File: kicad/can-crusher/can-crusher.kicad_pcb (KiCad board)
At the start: 2 copper layers, 100 x 100 mm, 21 parts, among them J1 Stepper Right, J2 Control UART, J3 Ext power, J4 Stepper Left, J5 Barrel_Jack, J6 Expansion Port, Q1 IRF9540N, Q2 BS170, SW1 Reboot, SW2 User Interaction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

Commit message: Add pull down to power circuitry
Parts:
- added R8: 57.6k, Resistor_THT:R_Axial_DIN0207_L6.3mm_D2.5mm_P10.16mm_Horizontal, F.Cu at (175.3, 105.4)
- R6: value 50k -> 57.6k
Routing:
- net Net-(Q2-Pad2): track 129.9 -> 140.6 mm
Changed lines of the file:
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@@
       (effects (font (size 1 1) (thickness 0.15)))
     )
-    (fp_text value "50k" (at 7.62 -2.54) (layer "F.Fab")
+    (fp_text value "57.6k" (at 7.62 -2.54) (layer "F.Fab")
       (effects (font (size 1 1) (thickness 0.15)))
     )
@@
       (net 1 "GND") (pinfunction "Pin_2") (pintype "passive"))
     (model "${KICAD6_3DMODEL_DIR}/Connector_PinHeader_2.54mm.3dshapes/PinHeader_1x02_P2.54mm_Vertical.wrl"
+      (offset (xyz 0 0 0))
+      (scale (xyz 1 1 1))
+      (rotate (xyz 0 0 0))
+    )
+  )
+  (footprint "Resistor_THT:R_Axial_DIN0207_L6.3mm_D2.5mm_P10.16mm_Horizontal" (layer "F.Cu")
+    (at 175.26 105.41)
+    (descr "Resistor, Axial_DIN0207 series, Axial, Horizontal, pin pitch=10.16mm, 0.25W = 1/4W, length*diameter=6.3*2.5mm^2, http://cdn-reichelt.de/documents/datenblatt/B400/1_4W%23YAG.pdf")
+    (tags "Resistor Axial_DIN0207 series Axial Horizontal pin pitch 10.16mm 0.25W = 1/4W length 6.3mm diameter 2.5mm")
+    (property "Sheetfile" "File: can-crusher.kicad_sch")
+    (property "Sheetname" "")
+    (attr through_hole)
+    (fp_text reference "R8" (at 5.08 -2.37) (layer "F.SilkS")
+      (effects (font (size 1 1) (thickness 0.15)))
+    )
+    (fp_text value "57.6k" (at 5.08 2.37) (layer "F.Fab")
+      (effects (font (size 1 1) (thickness 0.15)))
+    )
+    (fp_text user "${REFERENCE}" (at 5.08 0) (layer "F.Fab")
+      (effects (font (size 1 1) (thickness 0.15)))
+    )
+    (fp_line (start 9.12 0) (end 8.35 0) (layer "F.SilkS") (width 0.12))
+    (fp_line (start 8.35 -1.37) (end 1.81 -1.37) (layer "F.SilkS") (width 0.12))
+    (fp_line (start 1.81 -1.37) (end 1.81 1.37) (layer "F.SilkS") (width 0.12))
+    (fp_line (start 1.04 0) (end 1.81 0) (layer "F.SilkS") (width 0.12))
+    (fp_line (start 1.81 1.37) (end 8.35 1.37) (layer "F.SilkS") (width 0.12))
+    (fp_line (start 8.35 1.37) (end 8.35 -1.37) (layer "F.SilkS") (width 0.12))
+    (fp_line (start 11.21 -1.5) (end -1.05 -1.5) (layer "F.CrtYd") (width 0.05))
+    (fp_line (start 11.21 1.5) (end 11.21 -1.5) (layer "F.CrtYd") (width 0.05))
+    (fp_line (start -1.05 -1.5) (end -1.05 1.5) (layer "F.CrtYd") (width 0.05))
+    (fp_line (start -1.05 1.5) (end 11.21 1.5) (layer "F.CrtYd") (width 0.05))
+    (fp_line (start 8.23 1.25) (end 8.23 -1.25) (layer "F.Fab") (width 0.1))
+    (fp_line (start 10.16 0) (end 8.23 0) (layer "F.Fab") (width 0.1))
+    (fp_line (start 1.93 -1.25) (end 1.93 1.25) (layer "F.Fab") (width 0.1))
+    (fp_line (start 0 0) (end 1.93 0) (layer "F.Fab") (width 0.1))
+    (fp_line (start 1.93 1.25) (end 8.23 1.25) (layer "F.Fab") (width 0.1))
+    (fp_line (start 8.23 -1.25) (end 1.93 -1.25) (layer "F.Fab") (width 0.1))
+    (pad "1" thru_hole circle (at 0 0) (size 1.6 1.6) (drill 0.8) (layers *.Cu *.Mask)
+      (net 27 "Net-(Q2-Pad2)") (pintype "passive"))
+    (pad "2" thru_hole oval (at 10.16 0) (size 1.6 1.6) (drill 0.8) (layers *.Cu *.Mask)
+      (net 1 "GND") (pintype "passive"))
+    (model "${KICAD6_3DMODEL_DIR}/Resistor_THT.3dshapes/R_Axial_DIN0207_L6.3mm_D2.5mm_P10.16mm_Horizontal.wrl"
       (offset (xyz 0 0 0))
       (scale (xyz 1 1 1))
@@
   (segment (start 183.92 97.16) (end 189 92.08) (width 0.25) (layer "F.Cu") (net 26))
   (segment (start 184.78 92.08) (end 189 92.08) (width 0.25) (layer "F.Cu") (net 26))
+  (segment (start 176.53 95.25) (end 176.53 104.14) (width 0.25) (layer "F.Cu") (net 27))
   (segment (start 175.26 80.01) (end 175.26 88.9) (width 0.25) (layer "F.Cu") (net 27))
   (segment (start 133.35 120.65) (end 130.81 118.11) (width 0.25) (layer "F.Cu") (net 27))
@@
   (segment (start 176.53 90.17) (end 176.53 95.25) (width 0.25) (layer "F.Cu") (net 27))
   (segment (start 138.43 120.65) (end 133.35 120.65) (width 0.25) (layer "F.Cu") (net 27))
+  (segment (start 176.53 104.14) (end 175.26 105.41) (width 0.25) (layer "F.Cu") (net 27))
   (segment (start 130.81 115.57) (end 116.84 101.6) (width 0.25) (layer "F.Cu") (net 27))
   (segment (start 116.84 80.01) (end 120.65 76.2) (width 0.25) (layer "F.Cu") (net 27))
@@
     (connect_pads (clearance 0.508))
     (min_thickness 0.254) (filled_areas_thickness no)
-    (fill (thermal_gap 0.508) (thermal_bridge_width 0.508))
+    (fill yes (thermal_gap 0.508) (thermal_bridge_width 0.508))
     (polygon
       (pts

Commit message: Add mounting holes
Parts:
- added REF1: MountingHole_3mm_Pad, MountingHole:MountingHole_3mm_Pad, F.Cu at (101.6, 57.1)
- added REF2: MountingHole_3mm_Pad, MountingHole:MountingHole_3mm_Pad, F.Cu at (177.8, 57.1)
- added REF3: MountingHole_3mm_Pad, MountingHole:MountingHole_3mm_Pad, F.Cu at (191.8, 135.9)
- added REF4: MountingHole_3mm_Pad, MountingHole:MountingHole_3mm_Pad, F.Cu at (101.6, 146.1)
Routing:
- net +3.3V: track 179.5 -> 177.7 mm
- net GND: vias 22 -> 16
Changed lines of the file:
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@@
   (net 55 "Net-(D1-Pad2)")
   (net 56 "Net-(D1-Pad4)")
+  (footprint "MountingHole:MountingHole_3mm_Pad" (layer "F.Cu")
+    (at 191.77 135.89)
+    (descr "Mounting Hole 3mm")
+    (tags "mounting hole 3mm")
+    (attr exclude_from_pos_files exclude_from_bom)
+    (fp_text reference "REF3" (at 0 -4) (layer "Cmts.User")
+      (effects (font (size 1 1) (thickness 0.15)))
+    )
+    (fp_text value "MountingHole_3mm_Pad" (at 0 4) (layer "F.Fab")
+      (effects (font (size 1 1) (thickness 0.15)))
+    )
+    (fp_text user "${REFERENCE}" (at 0 0) (layer "F.Fab")
+      (effects (font (size 1 1) (thickness 0.15)))
+    )
+    (fp_circle (center 0 0) (end 3 0) (layer "Cmts.User") (width 0.15) (fill none))
+    (fp_circle (center 0 0) (end 3.25 0) (layer "F.CrtYd") (width 0.05) (fill none))
+    (pad "1" thru_hole circle (at 0 0) (size 6 6) (drill 3) (layers *.Cu *.Mask))
+  )
+  (footprint "MountingHole:MountingHole_3mm_Pad" (layer "F.Cu")
+    (at 177.8 57.15)
+    (descr "Mounting Hole 3mm")
+    (tags "mounting hole 3mm")
+    (attr exclude_from_pos_files exclude_from_bom)
+    (fp_text reference "REF2" (at 0 -4) (layer "Cmts.User")
+      (effects (font (size 1 1) (thickness 0.15)))
+    )
+    (fp_text value "MountingHole_3mm_Pad" (at 0 4) (layer "F.Fab")
+      (effects (font (size 1 1) (thickness 0.15)))
+    )
+    (fp_text user "${REFERENCE}" (at 0 0) (layer "F.Fab")
+      (effects (font (size 1 1) (thickness 0.15)))
+    )
+    (fp_circle (center 0 0) (end 3 0) (layer "Cmts.User") (width 0.15) (fill none))
+    (fp_circle (center 0 0) (end 3.25 0) (layer "F.CrtYd") (width 0.05) (fill none))
+    (pad "1" thru_hole circle (at 0 0) (size 6 6) (drill 3) (layers *.Cu *.Mask))
+  )
   (footprint "Package_TO_SOT_THT:TO-220-3_Vertical" (layer "F.Cu")
     (at 189 92.08 90)
@@
       (rotate (xyz 0 0 0))
     )
+  )
+  (footprint "MountingHole:MountingHole_3mm_Pad" (layer "F.Cu")
+    (at 101.6 146.05)
+    (descr "Mounting Hole 3mm")
+    (tags "mounting hole 3mm")
+    (attr exclude_from_pos_files exclude_from_bom)
+    (fp_text reference "REF4" (at 0 -4) (layer "Cmts.User")
+      (effects (font (size 1 1) (thickness 0.15)))
+    )
+    (fp_text value "MountingHole_3mm_Pad" (at 0 4) (layer "F.Fab")
+      (effects (font (size 1 1) (thickness 0.15)))
+    )
+    (fp_text user "${REFERENCE}" (at 0 0) (layer "F.Fab")
+      (effects (font (size 1 1) (thickness 0.15)))
+    )
+    (fp_circle (center 0 0) (end 3 0) (layer "Cmts.User") (width 0.15) (fill none))
+    (fp_circle (center 0 0) (end 3.25 0) (layer "F.CrtYd") (width 0.05) (fill none))
+    (pad "1" thru_hole circle (at 0 0) (size 6 6) (drill 3) (layers *.Cu *.Mask))
   )
   (footprint "Button_Switch_THT:SW_PUSH_6mm_H4.3mm" (layer "F.Cu")
@@
     )
   )
+  (footprint "MountingHole:MountingHole_3mm_Pad" (layer "F.Cu")
+    (at 101.6 57.15)
+    (descr "Mounting Hole 3mm")
+    (tags "mounting hole 3mm")
+    (attr exclude_from_pos_files exclude_from_bom)
+    (fp_text reference "REF1" (at 0 -4) (layer "Cmts.User")
+      (effects (font (size 1 1) (thickness 0.15)))
+    )
+    (fp_text value "MountingHole_3mm_Pad" (at 0 4) (layer "F.Fab")
+      (effects (font (size 1 1) (thickness 0.15)))
+    )
+    (fp_text user "${REFERENCE}" (at 0 0) (layer "F.Fab")
+      (effects (font (size 1 1) (thickness 0.15)))
+    )
+    (fp_circle (center 0 0) (end 3 0) (layer "Cmts.User") (width 0.15) (fill none))
+    (fp_circle (center 0 0) (end 3.25 0) (layer "F.CrtYd") (width 0.05) (fill none))
+    (pad "1" thru_hole circle (at 0 0) (size 6 6) (drill 3) (layers *.Cu *.Mask))
+  )
   (footprint "Resistor_THT:R_Axial_DIN0207_L6.3mm_D2.5mm_P10.16mm_Horizontal" (layer "F.Cu")
     (at 194.08 99 180)
@@
   )
   (gr_rect (start 97 51) (end 197 151) (layer "Edge.Cuts") (width 0.1) (fill none))
-  (gr_text "JLCJLCJLCJLC" (at 106.68 53.34) (layer "B.SilkS")
+  (gr_text "JLCJLCJLCJLC" (at 113.03 97.79 90) (layer "B.SilkS")
     (effects (font (size 1 1) (thickness 0.15)) (justify mirror))
   )
-  (gr_text "${COMPANY}\n" (at 165.1 55.88) (layer "B.SilkS")
+  (gr_text "${COMPANY}\n" (at 109.22 97.79 90) (layer "B.SilkS")
     (effects (font (size 1 1) (thickness 0.15)) (justify mirror))
   )
-  (gr_text "${TITLE}\n" (at 175.26 53.34) (layer "B.SilkS")
+  (gr_text "${TITLE}\n" (at 100.33 96.52 90) (layer "B.SilkS")
     (effects (font (size 2 2) (thickness 0.3)) (justify mirror))
   )
-  (gr_text "${ISSUE_DATE} - Rev ${REVISION}" (at 133.35 53.34) (layer "B.SilkS")
+  (gr_text "${ISSUE_DATE} - Rev ${REVISION}" (at 105.41 97.79 90) (layer "B.SilkS")
     (effects (font (size 2 2) (thickness 0.3)) (justify mirror))
   )
   (via (at 129.54 140.97) (size 0.8) (drill 0.4) (layers "F.Cu" "B.Cu") (free) (net 1))
-  (via (at 104.14 92.71) (size 0.8) (drill 0.4) (layers "F.Cu" "B.Cu") (free) (net 1))
   (via (at 101.6 121.92) (size 0.8) (drill 0.4) (layers "F.Cu" "B.Cu") (free) (net 1))
   (via (at 148.59 114.3) (size 0.8) (drill 0.4) (layers "F.Cu" "B.Cu") (free) (net 1))
   (via (at 147.32 59.69) (size 0.8) (drill 0.4) (layers "F.Cu" "B.Cu") (free) (net 1))
-  (via (at 100.33 144.78) (size 0.8) (drill 0.4) (layers "F.Cu" "B.Cu") (free) (net 1))
   (via (at 121.92 111.76) (size 0.8) (drill 0.4) (layers "F.Cu" "B.Cu") (free) (net 1))
   (via (at 144.78 128.27) (size 0.8) (drill 0.4) (layers "F.Cu" "B.Cu") (free) (net 1))
-  (via (at 177.8 59.69) (size 0.8) (drill 0.4) (layers "F.Cu" "B.Cu") (free) (net 1))
   (via (at 173.99 138.43) (size 0.8) (drill 0.4) (layers "F.Cu" "B.Cu") (free) (net 1))
   (via (at 149.86 120.65) (size 0.8) (drill 0.4) (layers "F.Cu" "B.Cu") (free) (net 1))
   (via (at 181.61 102.87) (size 0.8) (drill 0.4) (layers "F.Cu" "B.Cu") (free) (net 1))
   (via (at 190.5 118.11) (size 0.8) (drill 0.4) (layers "F.Cu" "B.Cu") (free) (net 1))
-  (via (at 102.87 81.28) (size 0.8) (drill 0.4) (layers "F.Cu" "B.Cu") (free) (net 1))
   (via (at 116.84 59.69) (size 0.8) (drill 0.4) (layers "F.Cu" "B.Cu") (free) (net 1))
   (via (at 190.5 107.95) (size 0.8) (drill 0.4) (layers "F.Cu" "B.Cu") (free) (net 1))
-  (via (at 105.41 59.69) (size 0.8) (drill 0.4) (layers "F.Cu" "B.Cu") (free) (net 1))
-  (via (at 193.04 135.89) (size 0.8) (drill 0.4) (layers "F.Cu" "B.Cu") (free) (net 1))
   (via (at 109.22 119.38) (size 0.8) (drill 0.4) (layers "F.Cu" "B.Cu") (free) (net 1))
   (via (at 147.32 81.28) (size 0.8) (drill 0.4) (layers "F.Cu" "B.Cu") (free) (net 1))
@@
   (segment (start 138.43 135.89) (end 123.19 135.89) (width 0.25) (layer "F.Cu") (net 22))
   (segment (start 123.19 135.89) (end 121.92 137.16) (width 0.25) (layer "F.Cu") (net 22))
+  (segment (start 105.41 149.86) (end 105.41 132.08) (width 0.25) (layer "F.Cu") (net 23))
+  (segment (start 137.16 74.93) (end 138.6025 73.4875) (width 0.25) (layer "F.Cu") (net 23))
   (segment (start 138.6025 73.8325) (end 138.6025 72.65) (width 0.25) (layer "F.Cu") (net 23))
+  (segment (start 121.92 149.86) (end 105.41 149.86) (width 0.25) (layer "F.Cu") (net 23))
   (segment (start 168.6025 73.9675) (end 167.64 74.93) (width 0.25) (layer "F.Cu") (net 23))
   (segment (start 167.64 74.93) (end 139.7 74.93) (width 0.25) (layer "F.Cu") (net 23))
+  (segment (start 105.41 132.08) (end 114.3 123.19) (width 0.25) (layer "F.Cu") (net 23))
+  (segment (start 119.38 74.93) (end 137.16 74.93) (width 0.25) (layer "F.Cu") (net 23))
   (segment (start 138.6025 73.4875) (end 138.6025 72.65) (width 0.25) (layer "F.Cu") (net 23))
-  (segment (start 114.3 80.01) (end 119.38 74.93) (width 0.25) (layer "F.Cu") (net 23))
   (segment (start 139.7 74.93) (end 138.6025 73.8325) (width 0.25) (layer "F.Cu") (net 23))
   (segment (start 124.46 138.43) (end 124.46 147.32) (width 0.25) (layer "F.Cu") (net 23))
+  (segment (start 114.3 80.01) (end 119.38 74.93) (width 0.25) (layer "F.Cu") (net 23))
   (segment (start 138.43 138.43) (end 124.46 138.43) (width 0.25) (layer "F.Cu") (net 23))
   (segment (start 168.6025 72.65) (end 168.6025 73.9675) (width 0.25) (layer "F.Cu") (net 23))
-  (segment (start 121.92 149.86) (end 104.14 149.86) (width 0.25) (layer "F.Cu") (net 23))
   (segment (start 114.3 123.19) (end 114.3 80.01) (width 0.25) (layer "F.Cu") (net 23))
-  (segment (start 137.16 74.93) (end 138.6025 73.4875) (width 0.25) (layer "F.Cu") (net 23))
   (segment (start 124.46 147.32) (end 121.92 149.86) (width 0.25) (layer "F.Cu") (net 23))
-  (segment (start 104.14 133.35) (end 114.3 123.19) (width 0.25) (layer "F.Cu") (net 23))
-  (segment (start 119.38 74.93) (end 137.16 74.93) (width 0.25) (layer "F.Cu") (net 23))
-  (segment (start 104.14 149.86) (end 104.14 133.35) (width 0.25) (layer "F.Cu") (net 23))
   (segment (start 173.99 115.57) (end 177.8 115.57) (width 0.25) (layer "F.Cu") (net 24))
   (segment (start 177.8 115.57) (end 182.88 120.65) (width 0.25) (layer "F.Cu") (net 24))
@@
   (segment (start 184.78 92.08) (end 189 92.08) (width 0.25) (layer "F.Cu") (net 26))
   (segment (start 176.53 95.25) (end 176.53 104.14) (width 0.25) (layer "F.Cu") (net 27))
+  (segment (start 116.84 101.6) (end 116.84 80.01) (width 0.25) (layer "F.Cu") (net 27))
   (segment (start 175.26 80.01) (end 175.26 88.9) (width 0.25) (layer "F.Cu") (net 27))
   (segment (start 133.35 120.65) (end 130.81 118.11) (width 0.25) (layer "F.Cu") (net 27))
   (segment (start 171.45 76.2) (end 175.26 80.01) (width 0.25) (layer "F.Cu") (net 27))
-  (segment (start 116.84 101.6) (end 116.84 80.01) (width 0.25) (layer "F.Cu") (net 27))
   (segment (start 175.26 88.9) (end 176.53 90.17) (width 0.25) (layer "F.Cu") (net 27))
   (segment (start 120.65 76.2) (end 171.45 76.2) (width 0.25) (layer "F.Cu") (net 27))

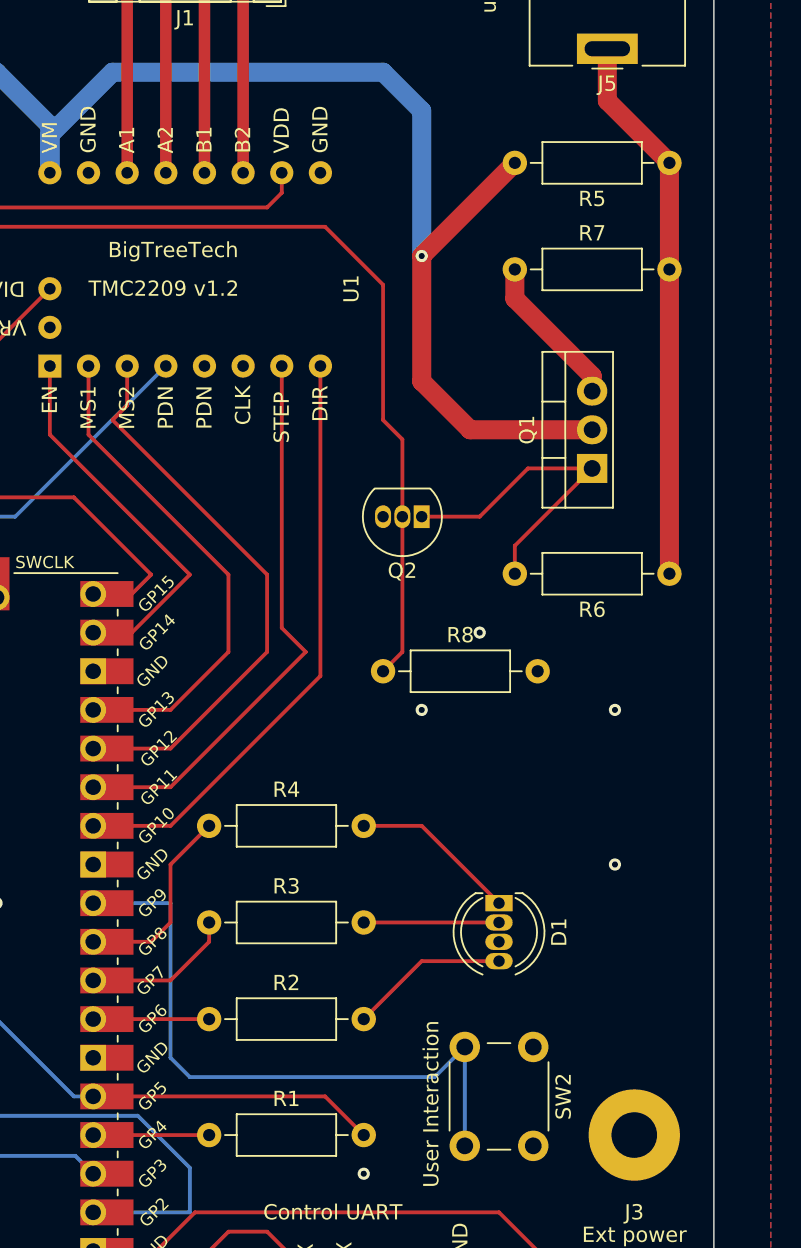
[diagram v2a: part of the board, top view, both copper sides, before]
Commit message: Start moving to SMD components
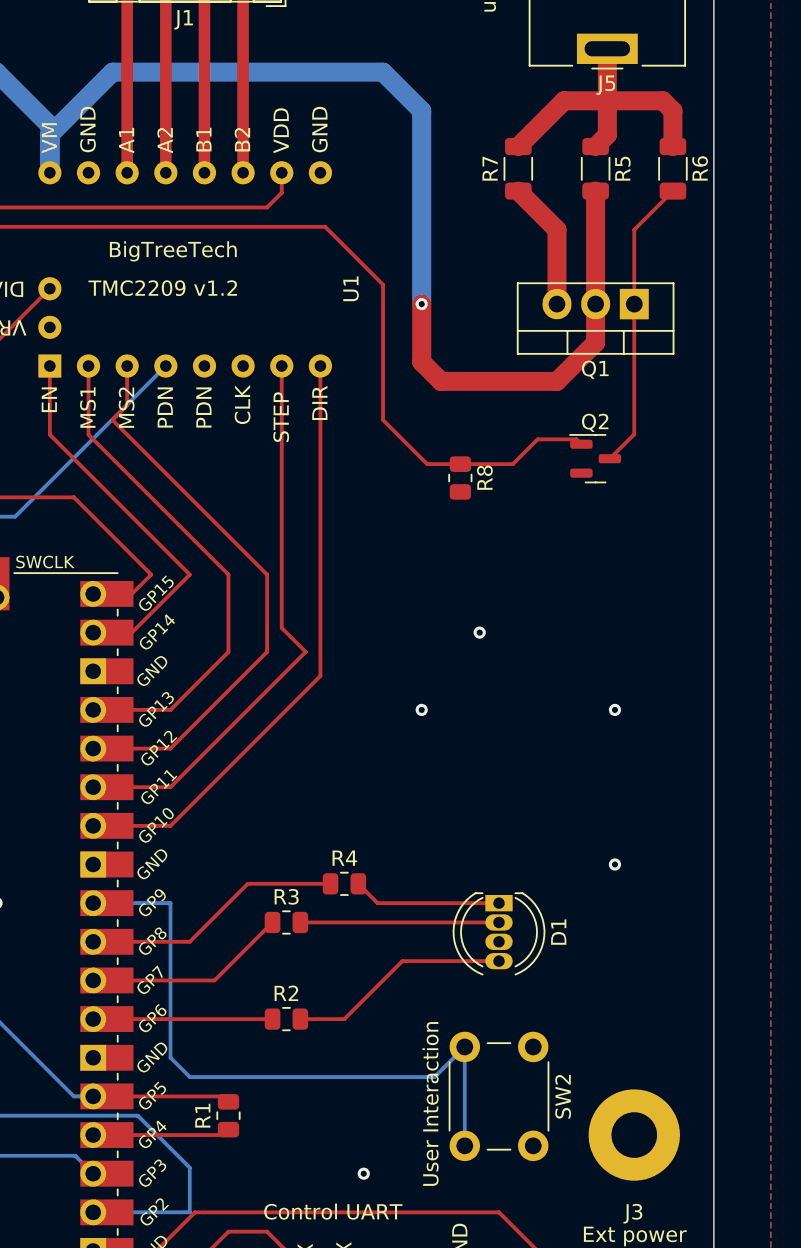
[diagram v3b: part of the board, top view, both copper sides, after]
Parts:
- Q2: value BS170 -> MMBF170; footprint Package_TO_SOT_THT:TO-92_Inline -> Package_TO_SOT_SMD:SOT-23
- R1, R2, R3, R4, R8: footprint Resistor_THT:R_Axial_DIN0207_L6.3mm_D2.5mm_P10.16mm_Horizontal -> Resistor_SMD:R_0805_2012Metric
- R5, R6, R7: footprint Resistor_THT:R_Axial_DIN0207_L6.3mm_D2.5mm_P10.16mm_Horizontal -> Resistor_SMD:R_1206_3216Metric
- moved R6 26.6 mm to (194.3, 72.4), turned to -90 degrees
- moved R8 13.7 mm to (180.3, 92.7), turned to -90 degrees
- moved Q2 12.0 mm to (189.2, 91.4), turned to 0 degrees
- moved Q1 11.1 mm to (191.8, 81.3), turned to 180 degrees
- moved R4 9.67 mm to (172.7, 119.4)
- moved R7 6.61 mm to (184.2, 72.4), turned to 90 degrees
- moved R2 5.08 mm to (168.9, 128.3)
- moved R3 5.08 mm to (168.9, 121.9)
- moved R5 4.87 mm to (189.2, 72.4), turned to -90 degrees
- moved R1 1.80 mm to (165.1, 134.6), turned to 90 degrees
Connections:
- Q2 pad 1: Net-(Q1-Pad1) -> Net-(R8-Pad1)
- Q2 pad 2: Net-(Q2-Pad2) -> GND
- Q2 pad 3: GND -> Net-(Q1-Pad1)
- R8 pad 1: Net-(Q2-Pad2) -> Net-(R8-Pad1)
- U2 pad 29: Net-(Q2-Pad2) -> Net-(R8-Pad1)
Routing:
- net Net-(Q2-Pad2): track 140.6 -> 0.00 mm
- net Net-(R8-Pad1): track 0.00 -> 138.1 mm
- net +12V: track 36.2 -> 20.8 mm
- net /STEP_TXRX: track 101.9 -> 92.1 mm
- net Net-(D1-Pad4): track 10.5 -> 14.6 mm
- net Net-(D1-Pad2): track 8.89 -> 13.1 mm
- net Net-(R2-Pad1): track 7.62 -> 11.8 mm
- net Net-(R4-Pad1): track 13.0 -> 17.2 mm
- net Net-(R3-Pad1): track 9.94 -> 13.4 mm
- net Net-(Q1-Pad1): track 21.5 -> 19.3 mm
- net Net-(Q1-Pad3): track 10.1 -> 8.48 mm
- net Net-(R1-Pad1): track 7.62 -> 9.04 mm
- net Net-(D1-Pad1): track 11.0 -> 9.77 mm
- net /12V_ON: track 108.4 -> 109.0 mm
